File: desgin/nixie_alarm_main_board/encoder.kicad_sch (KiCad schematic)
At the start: 7 parts

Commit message: filter caps
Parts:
- added C4: 100nF 25V, GRM033D70J224ME01D, symbol SamacSys_Parts:GRM033R71E101KA01J
- added R7: 10k, ERJUP6, symbol SamacSys_Parts:ERJ-UP6D5101V
- added R8: 1k, ERJUP6, symbol SamacSys_Parts:ERJ-UP6D5101V
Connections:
- net +5V: now also R7.2
- net ENC_SW: now also R8.2; no longer ENC1.S1
- net GND: now also C4.2
- new net: C4.1, ENC1.S1, R7.1, R8.1

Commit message: new caps footprint
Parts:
- C14, C15, C4: footprint GRM033D70J224ME01D -> Capacitor_SMD:C_0805_2012Metric_Pad1.18x1.45mm_HandSolder
- R17, R18, R19, R20, R7, R8: footprint ERJUP6 -> Resistor_SMD:R_0805_2012Metric_Pad1.20x1.40mm_HandSolder
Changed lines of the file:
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@@
 			)
 		)
-		(property "Footprint" "ERJUP6"
+		(property "Footprint" "Resistor_SMD:R_0805_2012Metric_Pad1.20x1.40mm_HandSolder"
 			(at 279.07 74.93 0)
 			(effects
@@
 			)
 		)
-		(property "Footprint" "GRM033D70J224ME01D"
+		(property "Footprint" "Capacitor_SMD:C_0805_2012Metric_Pad1.18x1.45mm_HandSolder"
 			(at 33.096 108.712 0)
 			(effects
@@
 			)
 		)
-		(property "Footprint" "ERJUP6"
+		(property "Footprint" "Resistor_SMD:R_0805_2012Metric_Pad1.20x1.40mm_HandSolder"
 			(at 251.892 75.692 0)
 			(effects
@@
 			)
 		)
-		(property "Footprint" "ERJUP6"
+		(property "Footprint" "Resistor_SMD:R_0805_2012Metric_Pad1.20x1.40mm_HandSolder"
 			(at 251.892 98.552 0)
 			(effects
@@
 			)
 		)
-		(property "Footprint" "ERJUP6"
+		(property "Footprint" "Resistor_SMD:R_0805_2012Metric_Pad1.20x1.40mm_HandSolder"
 			(at 134.62 -6.528 0)
 			(effects
@@
 			)
 		)
-		(property "Footprint" "ERJUP6"
+		(property "Footprint" "Resistor_SMD:R_0805_2012Metric_Pad1.20x1.40mm_HandSolder"
 			(at 196.85 185.852 0)
 			(effects
@@
 			)
 		)
-		(property "Footprint" "GRM033D70J224ME01D"
+		(property "Footprint" "Capacitor_SMD:C_0805_2012Metric_Pad1.18x1.45mm_HandSolder"
 			(at 225.476 75.438 0)
 			(effects
@@
 			)
 		)
-		(property "Footprint" "ERJUP6"
+		(property "Footprint" "Resistor_SMD:R_0805_2012Metric_Pad1.20x1.40mm_HandSolder"
 			(at 134.62 -1.448 0)
 			(effects
@@
 			)
 		)
-		(property "Footprint" "GRM033D70J224ME01D"
+		(property "Footprint" "Capacitor_SMD:C_0805_2012Metric_Pad1.18x1.45mm_HandSolder"
 			(at 86.69 98.806 0)
 			(effects

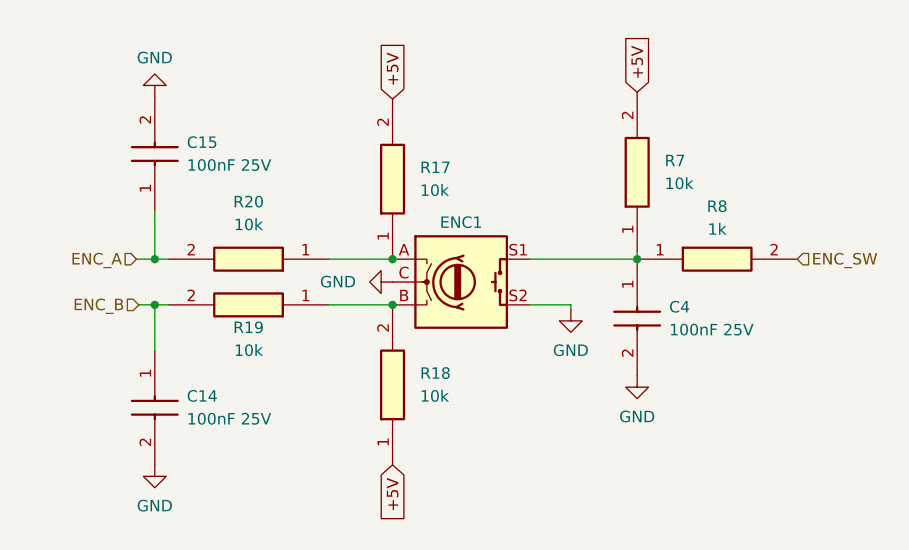
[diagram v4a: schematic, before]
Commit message: all components in board footprint
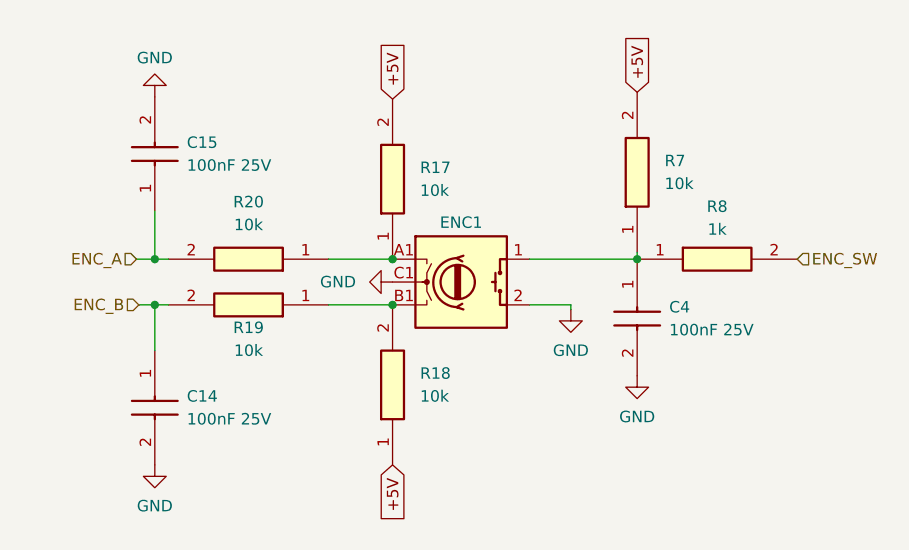
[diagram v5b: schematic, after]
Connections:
- net GND: now also ENC1.2, ENC1.C1; no longer ENC1.C, ENC1.S2
- net at C4.1, R7.1, R8.1: now also ENC1.1; no longer ENC1.S1
- net at R17.1, R20.1: now also ENC1.A1; no longer ENC1.A
- net at R18.2, R19.1: now also ENC1.B1; no longer ENC1.B
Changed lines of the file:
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@@
 			)
 		)
-		(pin "A"
+		(pin "A1"
 		)
-		(pin "C"
+		(pin "2"
 		)
-		(pin "S1"
+		(pin "B1"
 		)
-		(pin "S2"
+		(pin "1"
 		)
-		(pin "B"
+		(pin "C1"
 		)
 		(instances

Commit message: fixes added
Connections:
- net GND: now also ENC1.MH1, ENC1.MH2 (MH12)
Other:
- moved on the sheet: C14, C15, C4, R17, R18, R19, R20, R7, R8
